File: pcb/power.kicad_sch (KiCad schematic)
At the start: 39 parts, among them J4 Conn_01x02_Socket, U3 TPS63802DLAR, U4 BQ24078RGTR, U6 SN74LVC1G79DBVT

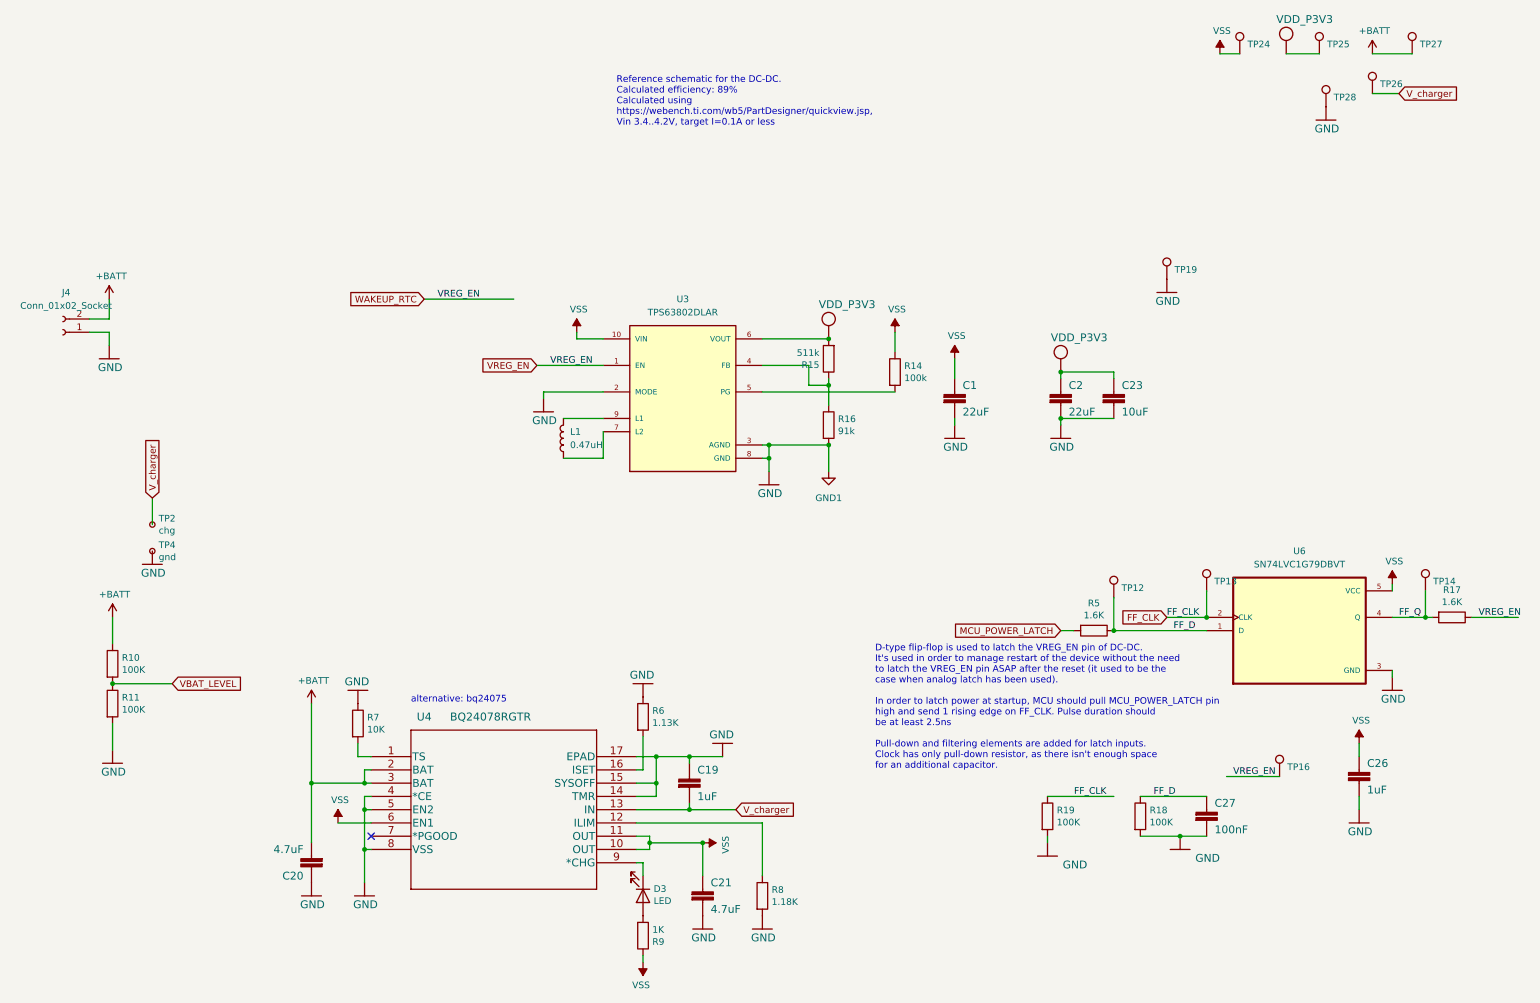
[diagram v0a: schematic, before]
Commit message: fixed couple issues with DF 1.4 (FF_CLK not propagated, RTC_INTR output inverted)
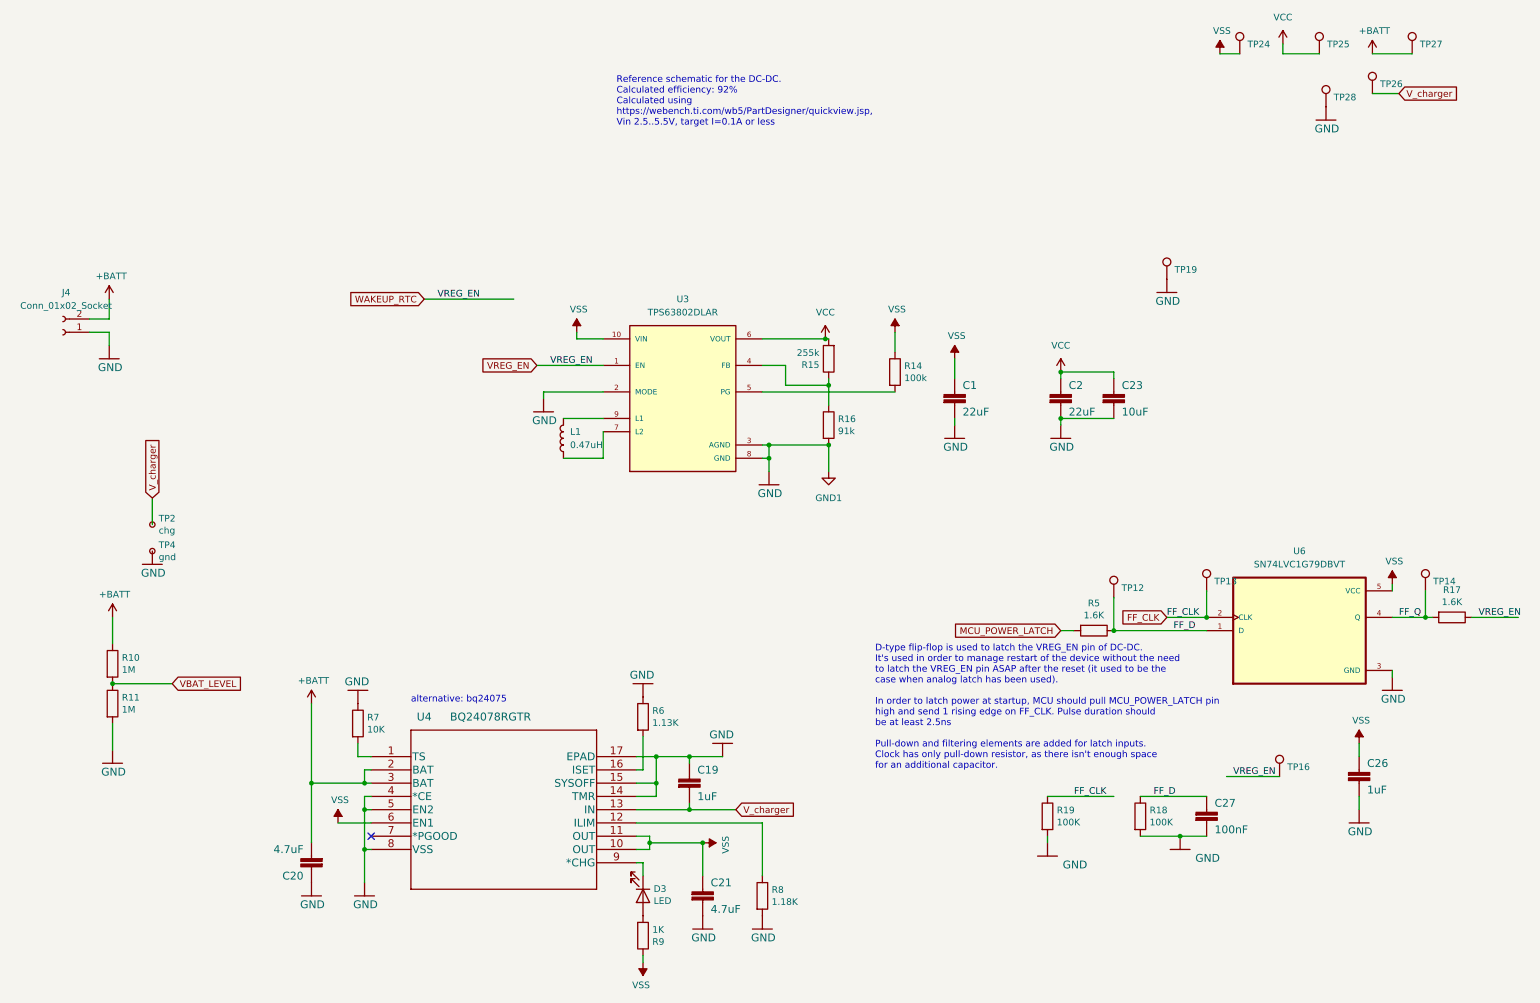
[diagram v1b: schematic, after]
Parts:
- R10, R11: value 100K -> 1M; LCSC C25741 -> C226699
- R15: value 511k -> 255k; LCSC C188257 -> C728604
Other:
- note added: "Reference schematic for the DC-DC. Calculated efficiency: 92% Calculated using https://webench.ti.com/wb5/PartDesigner/quickview.jsp, Vin 2.5..5.5V, target I=0.1A or less"
- note removed: "Reference schematic for the DC-DC. Calculated efficiency: 89% Calculated using https://webench.ti.com/wb5/PartDesigner/quickview.jsp, Vin 3.4..4.2V, target I=0.1A or less"
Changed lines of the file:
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@@
 (kicad_sch (version 20230121) (generator eeschema)
   (paper "A4")
-  (junction (at 162.56 67.31) (diameter 0) (color 0 0 0 0)
-  )
   (junction (at 276.86 120.65) (diameter 0) (color 0 0 0 0)
   )
+  (junction (at 161.925 67.31) (diameter 0) (color 0 0 0 0)
+  )
+  (junction (at 73.66 152.4) (diameter 0) (color 0 0 0 0)
+  )
+  (junction (at 25.4 133.35) (diameter 0) (color 0 0 0 0)
+  )
   (junction (at 207.01 73.66) (diameter 0) (color 0 0 0 0)
-  )
-  (junction (at 73.66 152.4) (diameter 0) (color 0 0 0 0)
-  )
-  (junction (at 25.4 133.35) (diameter 0) (color 0 0 0 0)
   )
   (junction (at 73.66 157.48) (diameter 0) (color 0 0 0 0)
@@
     (stroke (width 0) (type default))
   )
-  (wire (pts (xy 149.86 72.39) (xy 158.75 72.39))
+  (wire (pts (xy 149.86 72.39) (xy 154.305 72.39))
     (stroke (width 0) (type default))
   )
@@
     (stroke (width 0) (type default))
   )
+  (wire (pts (xy 249.555 10.795) (xy 249.555 12.7))
+    (stroke (width 0) (type default))
+  )
   (wire (pts (xy 135.89 157.48) (xy 144.78 157.48))
     (stroke (width 0) (type default))
@@
     (stroke (width 0) (type default))
   )
-  (wire (pts (xy 149.86 67.31) (xy 162.56 67.31))
+  (wire (pts (xy 149.86 67.31) (xy 161.925 67.31))
     (stroke (width 0) (type default))
   )
@@
     (stroke (width 0) (type default))
   )
-  (wire (pts (xy 250.19 12.7) (xy 256.54 12.7))
-    (stroke (width 0) (type default))
-  )
   (wire (pts (xy 162.56 76.2) (xy 162.56 80.01))
     (stroke (width 0) (type default))
@@
     (stroke (width 0) (type default))
   )
+  (wire (pts (xy 161.925 67.31) (xy 162.56 67.31))
+    (stroke (width 0) (type default))
+  )
   (wire (pts (xy 238.76 151.13) (xy 248.92 151.13))
     (stroke (width 0) (type default))
   )
+  (wire (pts (xy 249.555 12.7) (xy 256.54 12.7))
+    (stroke (width 0) (type default))
+  )
   (wire (pts (xy 106.68 72.39) (xy 119.38 72.39))
     (stroke (width 0) (type default))
@@
     (stroke (width 0) (type default))
   )
-  (wire (pts (xy 158.75 72.39) (xy 158.75 76.2))
-    (stroke (width 0) (type default))
-  )
-  (wire (pts (xy 158.75 76.2) (xy 162.56 76.2))
+  (wire (pts (xy 154.305 72.39) (xy 154.305 76.2))
+    (stroke (width 0) (type default))
+  )
+  (wire (pts (xy 154.305 76.2) (xy 162.56 76.2))
     (stroke (width 0) (type default))
   )
@@
     (effects (font (size 1.27 1.27)) (justify left bottom))
   )
-  (text "Reference schematic for the DC-DC.\nCalculated efficiency: 89%\nCalculated using \nhttps://webench.ti.com/wb5/PartDesigner/quickview.jsp,\nVin 3.4..4.2V, target I=0.1A or less"
+  (text "Reference schematic for the DC-DC.\nCalculated efficiency: 92%\nCalculated using \nhttps://webench.ti.com/wb5/PartDesigner/quickview.jsp,\nVin 2.5..5.5V, target I=0.1A or less"
     (at 121.92 26.67 0)
     (effects (font (size 1.27 1.27)) (justify left bottom))
@@
       (effects (font (size 1.27 1.27)) (justify left))
     )
-    (property "Value" "100K" (at 27.178 130.683 0)
+    (property "Value" "1M" (at 27.178 130.683 0)
       (effects (font (size 1.27 1.27)) (justify left))
     )
@@
       (effects (font (size 1.27 1.27)) hide)
     )
-    (property "LCSC" "C25741" (at 25.4 129.54 0)
+    (property "LCSC" "C226699" (at 25.4 129.54 0)
+      (effects (font (size 1.27 1.27)) hide)
+    )
+    (property "Populate" "" (at 25.4 129.54 0)
       (effects (font (size 1.27 1.27)) hide)
     )
@@
       (effects (font (size 1.27 1.27)) (justify left))
     )
-    (property "Value" "100K" (at 27.178 138.303 0)
+    (property "Value" "1M" (at 27.178 138.303 0)
       (effects (font (size 1.27 1.27)) (justify left))
     )
@@
       (effects (font (size 1.27 1.27)) hide)
     )
-    (property "LCSC" "C25741" (at 25.4 137.16 0)
+    (property "LCSC" "C226699" (at 25.4 137.16 0)
+      (effects (font (size 1.27 1.27)) hide)
+    )
+    (property "Populate" "" (at 25.4 137.16 0)
       (effects (font (size 1.27 1.27)) hide)
     )
@@
     )
   )
-  (symbol (lib_id "nRF52832_qfaa-eagle-import:VCC") (at 250.19 10.16 0) (unit 1)
-    (in_bom yes) (on_board yes) (dnp no)
-    (property "Reference" "#VDD_NRF0102" (at 250.19 10.16 0)
-      (effects (font (size 1.27 1.27)) hide)
-    )
-    (property "Value" "VDD_P3V3" (at 248.285 6.985 0)
-      (effects (font (size 1.4986 1.4986)) (justify left bottom))
-    )
-    (property "Footprint" "" (at 250.19 10.16 0)
-      (effects (font (size 1.27 1.27)) hide)
-    )
-    (property "Datasheet" "" (at 250.19 10.16 0)
-      (effects (font (size 1.27 1.27)) hide)
-    )
-    (pin "1")
-    (instances
-      (project "nRF52832_qfaa"
-        (path "/109caac1-5036-4f23-9a66-f569d871501b/00000000-0000-0000-0000-000061764c1f"
-          (reference "#VDD_NRF0102") (unit 1)
-        )
-      )
-    )
-  )
   (symbol (lib_id "power:VSS") (at 175.26 66.04 0) (unit 1)
     (in_bom yes) (on_board yes) (dnp no)
@@
       (effects (font (size 1.27 1.27)) (justify left))
     )
-    (property "Value" "511k" (at 160.782 69.977 0)
+    (property "Value" "255k" (at 160.782 69.977 0)
       (effects (font (size 1.27 1.27)) (justify left))
     )
@@
       (effects (font (size 1.27 1.27)) hide)
     )
-    (property "LCSC" "C188257" (at 162.56 71.12 0)
+    (property "LCSC" "C728604" (at 162.56 71.12 0)
       (effects (font (size 1.27 1.27)) hide)
     )
@@
         (path "/109caac1-5036-4f23-9a66-f569d871501b/00000000-0000-0000-0000-000061764c1f"
           (reference "#GND0110") (unit 1)
+        )
+      )
+    )
+  )
+  (symbol (lib_id "power:VCC") (at 207.01 73.66 0) (unit 1)
+    (in_bom yes) (on_board yes) (dnp no) (fields_autoplaced)
+    (property "Reference" "#PWR036" (at 207.01 77.47 0)
+      (effects (font (size 1.27 1.27)) hide)
+    )
+    (property "Value" "VCC" (at 207.01 68.58 0)
+      (effects (font (size 1.27 1.27)))
+    )
+    (property "Footprint" "" (at 207.01 73.66 0)
+      (effects (font (size 1.27 1.27)) hide)
+    )
+    (property "Datasheet" "" (at 207.01 73.66 0)
+      (effects (font (size 1.27 1.27)) hide)
+    )
+    (pin "1")
+    (instances
+      (project "nRF52832_qfaa"
+        (path "/109caac1-5036-4f23-9a66-f569d871501b/00000000-0000-0000-0000-000061764c1f"
+          (reference "#PWR036") (unit 1)
+        )
+      )
+    )
+  )
+  (symbol (lib_id "power:VCC") (at 161.925 67.31 0) (unit 1)
+    (in_bom yes) (on_board yes) (dnp no) (fields_autoplaced)
+    (property "Reference" "#PWR037" (at 161.925 71.12 0)
+      (effects (font (size 1.27 1.27)) hide)
+    )
+    (property "Value" "VCC" (at 161.925 62.23 0)
+      (effects (font (size 1.27 1.27)))
+    )
+    (property "Footprint" "" (at 161.925 67.31 0)
+      (effects (font (size 1.27 1.27)) hide)
+    )
+    (property "Datasheet" "" (at 161.925 67.31 0)
+      (effects (font (size 1.27 1.27)) hide)
+    )
+    (pin "1")
+    (instances
+      (project "nRF52832_qfaa"
+        (path "/109caac1-5036-4f23-9a66-f569d871501b/00000000-0000-0000-0000-000061764c1f"
+          (reference "#PWR037") (unit 1)
         )
       )
@@
     )
     (property "LCSC" "C2845237" (at 134.62 77.47 0)
+      (effects (font (size 1.27 1.27)) hide)
+    )
+    (property "Populate" "" (at 134.62 77.47 0)
       (effects (font (size 1.27 1.27)) hide)
     )
@@
     )
   )
-  (symbol (lib_id "nRF52832_qfaa-eagle-import:VCC") (at 162.56 64.77 0) (unit 1)
-    (in_bom yes) (on_board yes) (dnp no)
-    (property "Reference" "#VDD_NRF0101" (at 162.56 64.77 0)
-      (effects (font (size 1.27 1.27)) hide)
-    )
-    (property "Value" "VDD_P3V3" (at 160.655 61.595 0)
-      (effects (font (size 1.4986 1.4986)) (justify left bottom))
-    )
-    (property "Footprint" "" (at 162.56 64.77 0)
-      (effects (font (size 1.27 1.27)) hide)
-    )
-    (property "Datasheet" "" (at 162.56 64.77 0)
-      (effects (font (size 1.27 1.27)) hide)
-    )
-    (pin "1")
-    (instances
-      (project "nRF52832_qfaa"
-        (path "/109caac1-5036-4f23-9a66-f569d871501b/00000000-0000-0000-0000-000061764c1f"
-          (reference "#VDD_NRF0101") (unit 1)
-        )
-      )
-    )
-  )
   (symbol (lib_id "nRF52832_qfaa-eagle-import:GND") (at 257.81 25.4 0) (mirror y) (unit 1)
     (in_bom yes) (on_board yes) (dnp no)
@@
     )
   )
+  (symbol (lib_id "power:VCC") (at 249.555 10.795 0) (unit 1)
+    (in_bom yes) (on_board yes) (dnp no) (fields_autoplaced)
+    (property "Reference" "#PWR038" (at 249.555 14.605 0)
+      (effects (font (size 1.27 1.27)) hide)
+    )
+    (property "Value" "VCC" (at 249.555 5.715 0)
+      (effects (font (size 1.27 1.27)))
+    )
+    (property "Footprint" "" (at 249.555 10.795 0)
+      (effects (font (size 1.27 1.27)) hide)
+    )
+    (property "Datasheet" "" (at 249.555 10.795 0)
+      (effects (font (size 1.27 1.27)) hide)
+    )
+    (pin "1")
+    (instances
+      (project "nRF52832_qfaa"
+        (path "/109caac1-5036-4f23-9a66-f569d871501b/00000000-0000-0000-0000-000061764c1f"
+          (reference "#PWR038") (unit 1)
+        )
+      )
+    )
+  )
   (symbol (lib_id "nRF52832_qfaa-eagle-import:GND") (at 204.47 166.37 0) (mirror y) (unit 1)
     (in_bom yes) (on_board yes) (dnp no)
@@
         )
       )
-    )
-  )
-  (symbol (lib_id "nRF52832_qfaa-eagle-import:VCC") (at 207.01 71.12 0) (unit 1)
-    (in_bom yes) (on_board yes) (dnp no)
-    (property "Reference" "#VDD_NRF0104" (at 207.01 71.12 0)
-      (effects (font (size 1.27 1.27)) hide)
-    )
-    (property "Value" "VDD_P3V3" (at 205.105 67.945 0)
-      (effects (font (size 1.4986 1.4986)) (justify left bottom))
-    )
-    (property "Footprint" "" (at 207.01 71.12 0)
-      (effects (font (size 1.27 1.27)) hide)
-    )
-    (property "Datasheet" "" (at 207.01 71.12 0)
-      (effects (font (size 1.27 1.27)) hide)
-    )
-    (pin "1")
-    (instances
-      (project "nRF52832_qfaa"
-        (path "/109caac1-5036-4f23-9a66-f569d871501b/00000000-0000-0000-0000-000061764c1f"
-          (reference "#VDD_NRF0104") (unit 1)
-        )
-      )

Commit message: Design Freeze DF 1.4
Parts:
- U3: footprint VREG_TPS63802DLAR -> df_components:VREG_TPS63802DLAR
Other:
- moved on the sheet: TP24, TP25, TP26, TP27, TP28

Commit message: prepared the df1.4 fabrication outputs
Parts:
- D3: LCSC C72043 -> C131282
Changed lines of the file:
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@@
       (effects (font (size 1.27 1.27)) hide)
     )
-    (property "LCSC" "C72043" (at 127 173.99 0)
+    (property "LCSC" "C131282" (at 127 173.99 0)
       (effects (font (size 1.27 1.27)) hide)
     )
+    (property "Populate" "" (at 127 173.99 0)
+      (effects (font (size 1.27 1.27)) hide)
+    )

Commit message: df 1.4.52840 ready for production
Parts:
- C19, C26: LCSC C52923 -> C77007
- R14: value 100k -> 100K
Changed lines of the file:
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@@
       (effects (font (size 1.27 1.27)) hide)
     )
-    (property "LCSC" "C52923" (at 135.89 151.13 0)
+    (property "LCSC" "C77007" (at 135.89 151.13 0)
       (effects (font (size 1.27 1.27)) hide)
     )
@@
       (effects (font (size 1.27 1.27)) hide)
     )
-    (pin "2")
-    (pin "1")
+    (pin "1")
+    (pin "2")
     (instances
       (project "dictofun"
@@
       (effects (font (size 1.27 1.27)) hide)
     )
-    (property "LCSC" "C52923" (at 264.16 149.86 0)
+    (property "LCSC" "C77007" (at 264.16 149.86 0)
       (effects (font (size 1.27 1.27)) hide)
     )
@@
       (effects (font (size 1.27 1.27)) (justify left))
     )
-    (property "Value" "100k" (at 177.038 74.803 0)
-      (effects (font (size 1.27 1.27)) (justify left))
-    )
+    (property "Value" "100K" (at 177.038 74.803 0)
+      (effects (font (size 1.27 1.27)) (justify left))
+    )
